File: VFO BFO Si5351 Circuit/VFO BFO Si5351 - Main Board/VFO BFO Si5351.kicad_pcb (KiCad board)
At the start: 2 copper layers, 126 x 59.5 mm, 34 parts, among them J1 I2C Bus, J10 VIN +12,8V, J11 GND +5V +9V +12, J12 VFO_Front_Pannel, J2 Band, J3 Mode, J4 AGC, J5 ATT, J6 BFO, J7 TX, J8 IN RTTY, J9 IN S_meter, M1 Si5351A module, U1 ESP32-DEVKITC-32D, U2 PCF8574AP, U3 LM7809, U4 LM7805, U5 24LC32

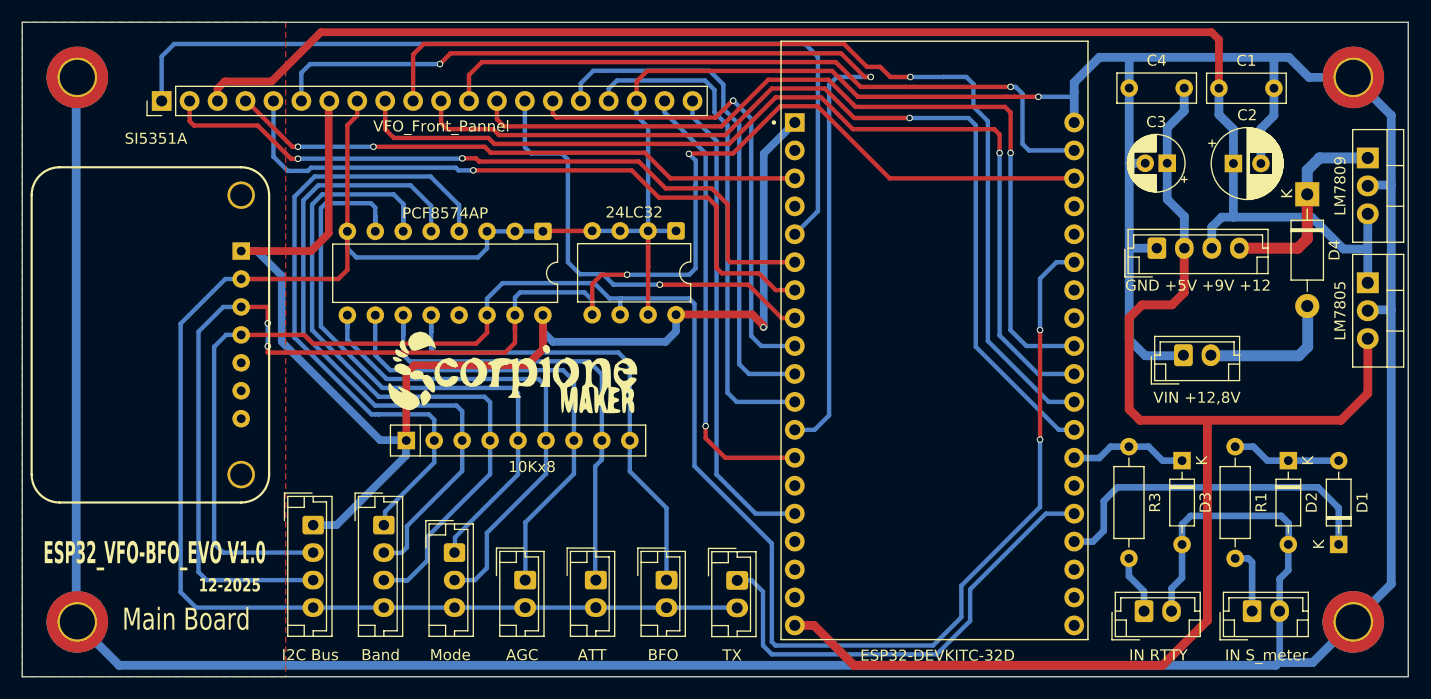
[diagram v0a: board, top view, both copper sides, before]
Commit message: PDF distenta componenti e  schemi elettrico e di montaggio
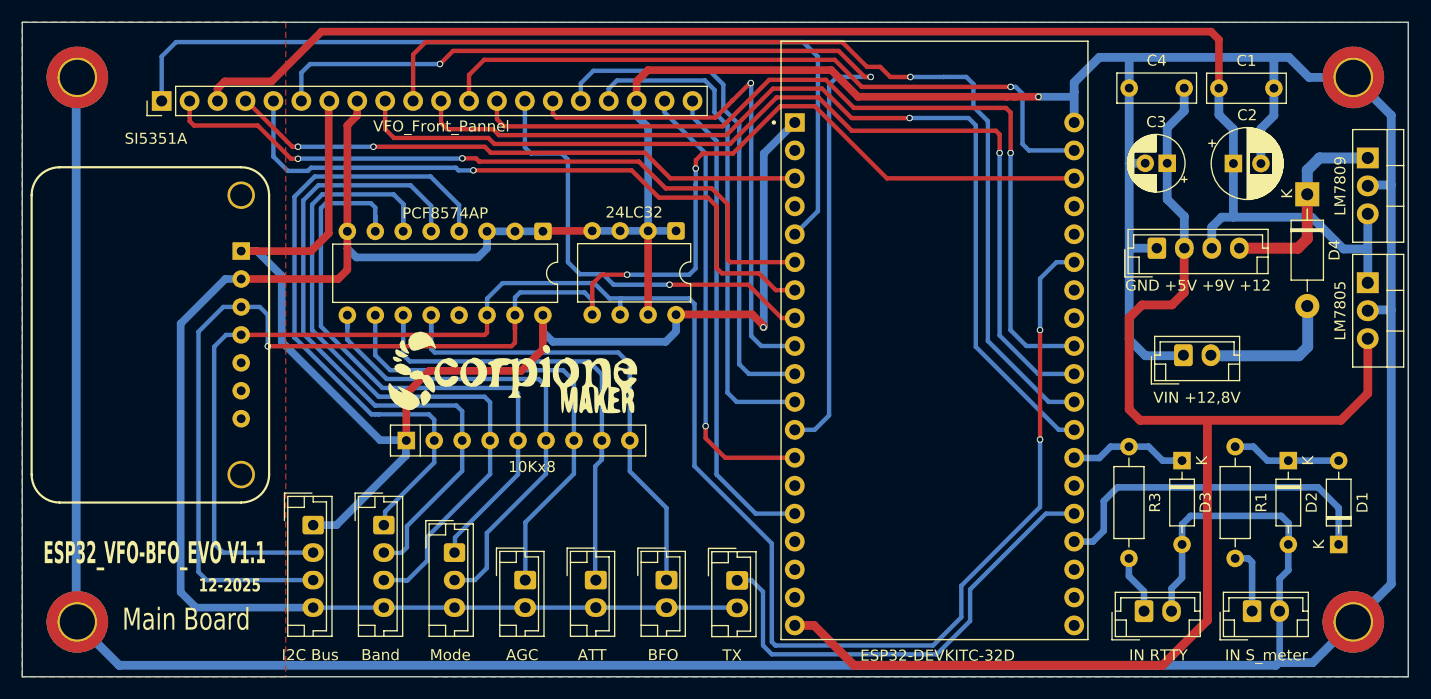
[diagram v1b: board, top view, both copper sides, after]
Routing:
- net GND: track 544.8 -> 541.5 mm
- net SW_MODE: track 44.7 -> 47.9 mm
- net SDA: track 144.0 -> 141.6 mm, vias 4 -> 3
- net SCL: track 170.0 -> 168.5 mm
- net +3.3V: track 130.7 -> 129.6 mm
- added copper zone on B.Cu, net GND
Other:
- board text added: "ESP32_VFO-BFO_EVO V1.1"
- board text removed: "ESP32_VFO-BFO_EVO V1.0"
